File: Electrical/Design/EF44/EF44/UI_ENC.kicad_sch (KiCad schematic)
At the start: 20 parts, among them U1 74HC165, U10 74HC4051, U2 74HC165, U9 74HC4051

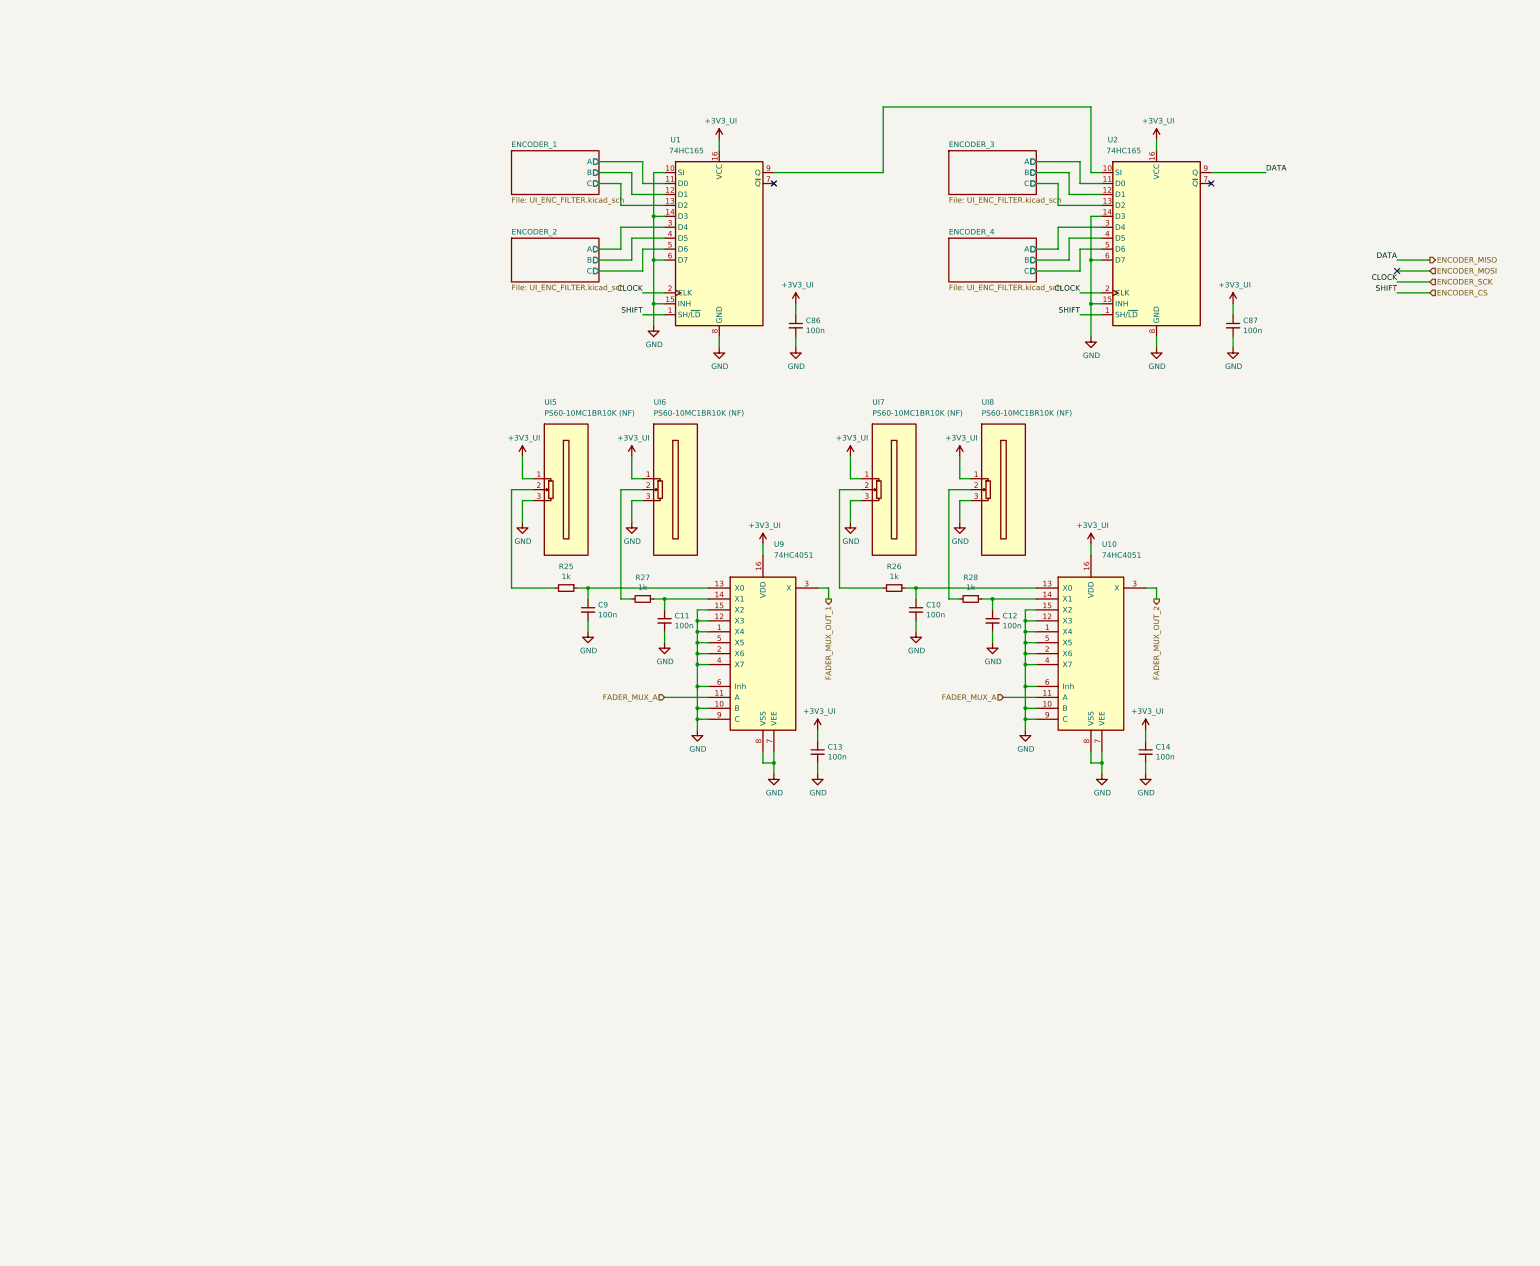
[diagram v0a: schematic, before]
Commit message: SUKU EF44 created from EN16 Base
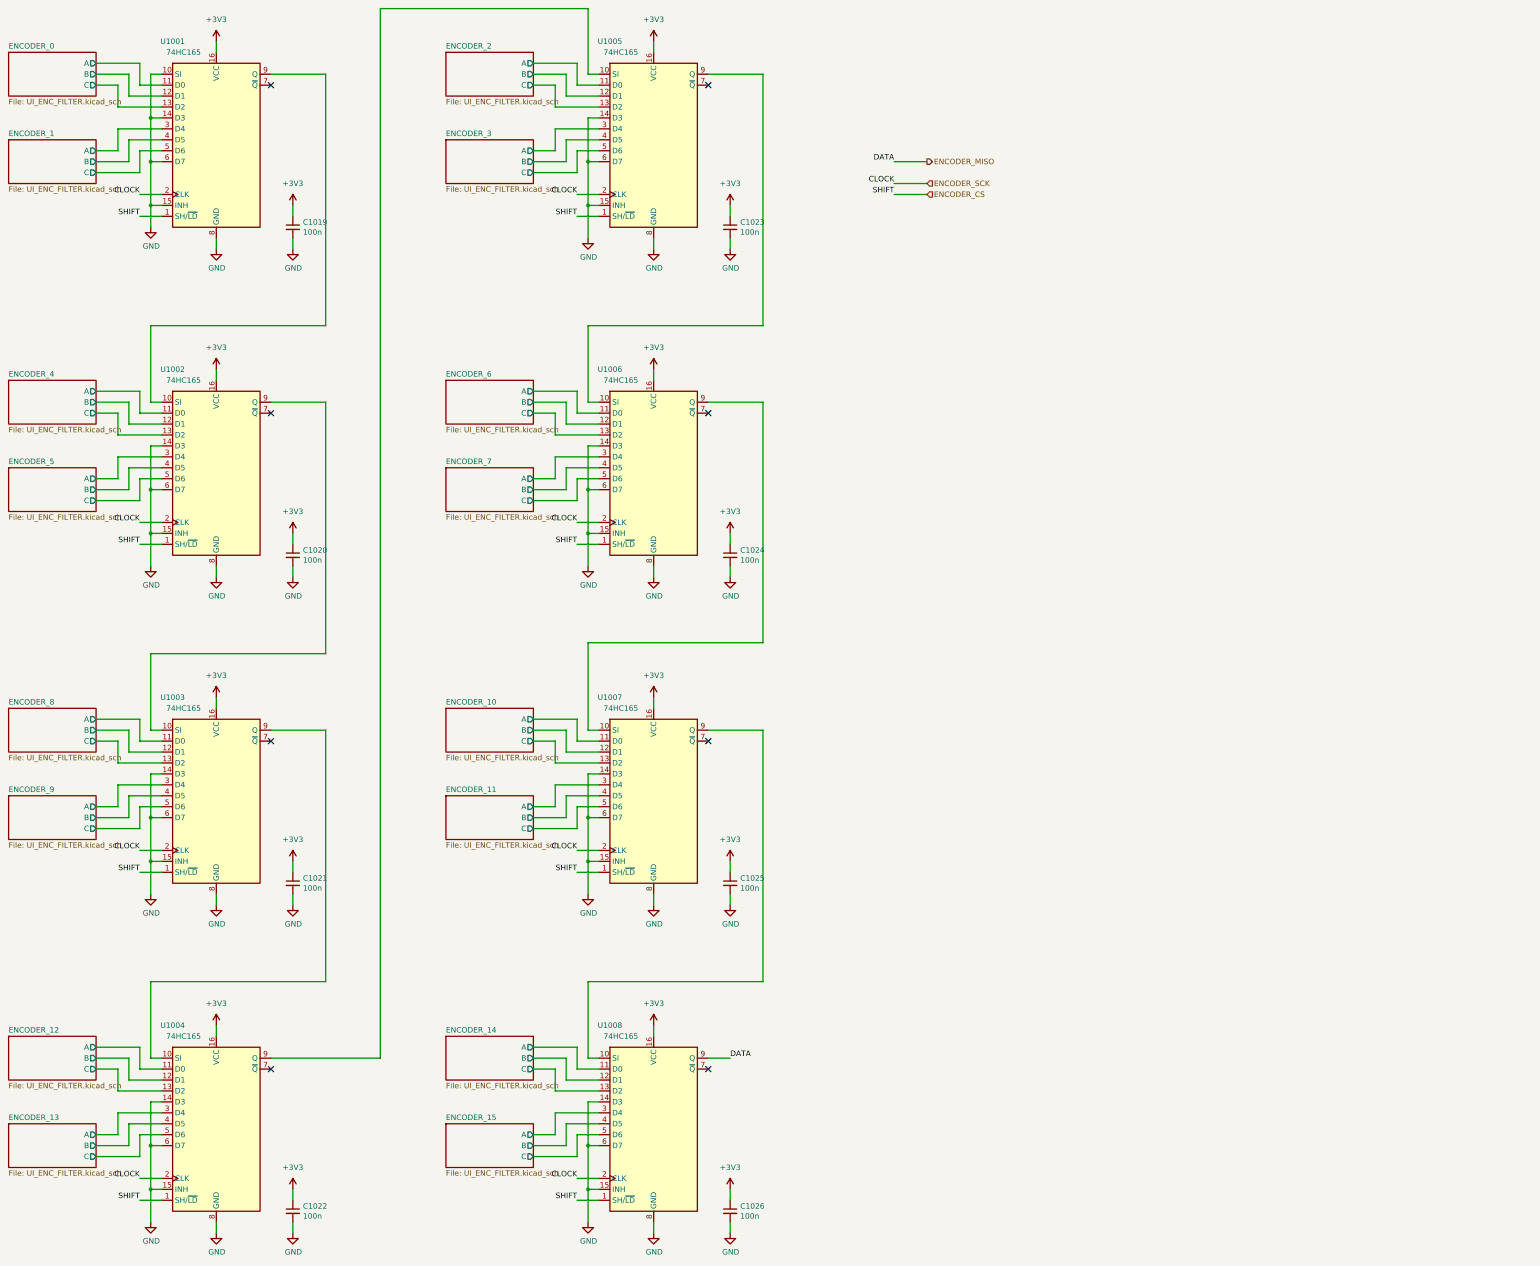
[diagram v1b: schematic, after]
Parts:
- removed C10, C11, C12, C13, C14, C9: 100n, suku_basics:CAP_0805, symbol suku_basics:CAP
- removed R25, R26, R27, R28: 1k, suku_basics:RES_0805, symbol suku_basics:RES
- removed U10, U9: 74HC4051, suku_basics:SOIC-16_74HC4051, symbol suku_basics:74HC4051
- removed UI5, UI6, UI7, UI8: PS60-10MC1BR10K (NF), suku_basics:UI_FADER_TT_long, symbol suku_basics:UI_Fader
- added C1020, C1021, C1022, C1024, C1025, C1026: 100n, suku_basics:CAP_0402, symbol suku_basics:CAP
- added U1002, U1003, U1004, U1006, U1007, U1008: 74HC165, suku_basics:SOIC-16_74HC165, symbol suku_basics:74HC165
- C1019: renamed from C86; footprint suku_basics:CAP_0805 -> suku_basics:CAP_0402
- C1023: renamed from C87; footprint suku_basics:CAP_0805 -> suku_basics:CAP_0402
- renumbered U1 to U1001, U2 to U1005
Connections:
- net ENCODER_1/A: now also U1001.3 (D4); no longer U1001.11 (D0)
- net ENCODER_1/B: now also U1001.4 (D5); no longer U1001.12 (D1)
- net ENCODER_1/C: now also U1001.5 (D6); no longer U1001.13 (D2)
- net ENCODER_2/A: now also U1005.11 (D0); no longer U1001.3 (D4)
- net ENCODER_2/B: now also U1005.12 (D1); no longer U1001.4 (D5)
- net ENCODER_2/C: now also U1005.13 (D2); no longer U1001.5 (D6)
- net ENCODER_3/A: now also U1005.3 (D4); no longer U1005.11 (D0)
- net ENCODER_3/B: now also U1005.4 (D5); no longer U1005.12 (D1)
- net ENCODER_3/C: now also U1005.5 (D6); no longer U1005.13 (D2)
- net ENCODER_4/A: now also U1002.11 (D0); no longer U1005.3 (D4)
- net ENCODER_4/B: now also U1002.12 (D1); no longer U1005.4 (D5)
- net ENCODER_4/C: now also U1002.13 (D2); no longer U1005.5 (D6)
- net ENCODER_CS: now also U1002.1 (SH/~{LD}), U1003.1 (SH/~{LD}), U1004.1 (SH/~{LD}), U1006.1 (SH/~{LD}), U1007.1 (SH/~{LD}), U1008.1 (SH/~{LD})
- net ENCODER_MISO: now also U1008.9 (Q); no longer U1005.9 (Q)
- net ENCODER_SCK: now also U1002.2 (CLK), U1003.2 (CLK), U1004.2 (CLK), U1006.2 (CLK), U1007.2 (CLK), U1008.2 (CLK)
- net GND: now also C1020.2, C1021.2, C1022.2, C1024.2, C1025.2, C1026.2, U1002.14 (D3), U1002.15 (INH), U1002.6 (D7), U1002.8 (GND), U1003.14 (D3), U1003.15 (INH), U1003.6 (D7), U1003.8 (GND), U1004.14 (D3), U1004.15 (INH), U1004.6 (D7), U1004.8 (GND), U1006.14 (D3), U1006.15 (INH), U1006.6 (D7), U1006.8 (GND), U1007.14 (D3), U1007.15 (INH), U1007.6 (D7), U1007.8 (GND), U1008.14 (D3), U1008.15 (INH), U1008.6 (D7), U1008.8 (GND)
- net at U1001.9 (Q): now also U1002.10 (SI); no longer U1005.10 (SI)
- net +3V3_UI renamed +3V3
- net +3V3: now also C1020.1, C1021.1, C1022.1, C1024.1, C1025.1, C1026.1, U1002.16 (VCC), U1003.16 (VCC), U1004.16 (VCC), U1006.16 (VCC), U1007.16 (VCC), U1008.16 (VCC)
- new net: U1002.9 (Q), U1003.10 (SI)
- new net: U1005.9 (Q), U1006.10 (SI)
- new net: U1006.9 (Q), U1007.10 (SI)
- new net: U1003.9 (Q), U1004.10 (SI)
- new net: U1007.9 (Q), U1008.10 (SI)
- new net: U1004.9 (Q), U1005.10 (SI)
- new net ENCODER_0/A: U1001.11 (D0)
- new net ENCODER_0/B: U1001.12 (D1)
- new net ENCODER_0/C: U1001.13 (D2)
- new net ENCODER_10/A: U1007.11 (D0)
- new net ENCODER_10/B: U1007.12 (D1)
- new net ENCODER_10/C: U1007.13 (D2)
- new net ENCODER_11/A: U1007.3 (D4)
- new net ENCODER_11/B: U1007.4 (D5)
- new net ENCODER_11/C: U1007.5 (D6)
- new net ENCODER_12/A: U1004.11 (D0)
- new net ENCODER_12/B: U1004.12 (D1)
- new net ENCODER_12/C: U1004.13 (D2)
- new net ENCODER_13/A: U1004.3 (D4)
- new net ENCODER_13/B: U1004.4 (D5)
- new net ENCODER_13/C: U1004.5 (D6)
- new net ENCODER_14/A: U1008.11 (D0)
- new net ENCODER_14/B: U1008.12 (D1)
- new net ENCODER_14/C: U1008.13 (D2)
- new net ENCODER_15/A: U1008.3 (D4)
- new net ENCODER_15/B: U1008.4 (D5)
- new net ENCODER_15/C: U1008.5 (D6)
- new net ENCODER_5/A: U1002.3 (D4)
- new net ENCODER_5/B: U1002.4 (D5)
- new net ENCODER_5/C: U1002.5 (D6)
- new net ENCODER_6/A: U1006.11 (D0)
- new net ENCODER_6/B: U1006.12 (D1)
- new net ENCODER_6/C: U1006.13 (D2)
- new net ENCODER_7/A: U1006.3 (D4)
- new net ENCODER_7/B: U1006.4 (D5)
- new net ENCODER_7/C: U1006.5 (D6)
- new net ENCODER_8/A: U1003.11 (D0)
- new net ENCODER_8/B: U1003.12 (D1)
- new net ENCODER_8/C: U1003.13 (D2)
- new net ENCODER_9/A: U1003.3 (D4)
- new net ENCODER_9/B: U1003.4 (D5)
- new net ENCODER_9/C: U1003.5 (D6)
- no-connect marks 3 -> 8
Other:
- added sheet ENCODER_0 (UI_ENC_FILTER.kicad_sch)
- added sheet ENCODER_10 (UI_ENC_FILTER.kicad_sch)
- added sheet ENCODER_11 (UI_ENC_FILTER.kicad_sch)
- added sheet ENCODER_12 (UI_ENC_FILTER.kicad_sch)
- added sheet ENCODER_13 (UI_ENC_FILTER.kicad_sch)
- added sheet ENCODER_14 (UI_ENC_FILTER.kicad_sch)
- added sheet ENCODER_15 (UI_ENC_FILTER.kicad_sch)
- added sheet ENCODER_5 (UI_ENC_FILTER.kicad_sch)
- added sheet ENCODER_6 (UI_ENC_FILTER.kicad_sch)
- added sheet ENCODER_7 (UI_ENC_FILTER.kicad_sch)
- added sheet ENCODER_8 (UI_ENC_FILTER.kicad_sch)
- added sheet ENCODER_9 (UI_ENC_FILTER.kicad_sch)
- moved on the sheet: C1019, C1023, U1001, U1005

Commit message: SUKU EF44 component positions done
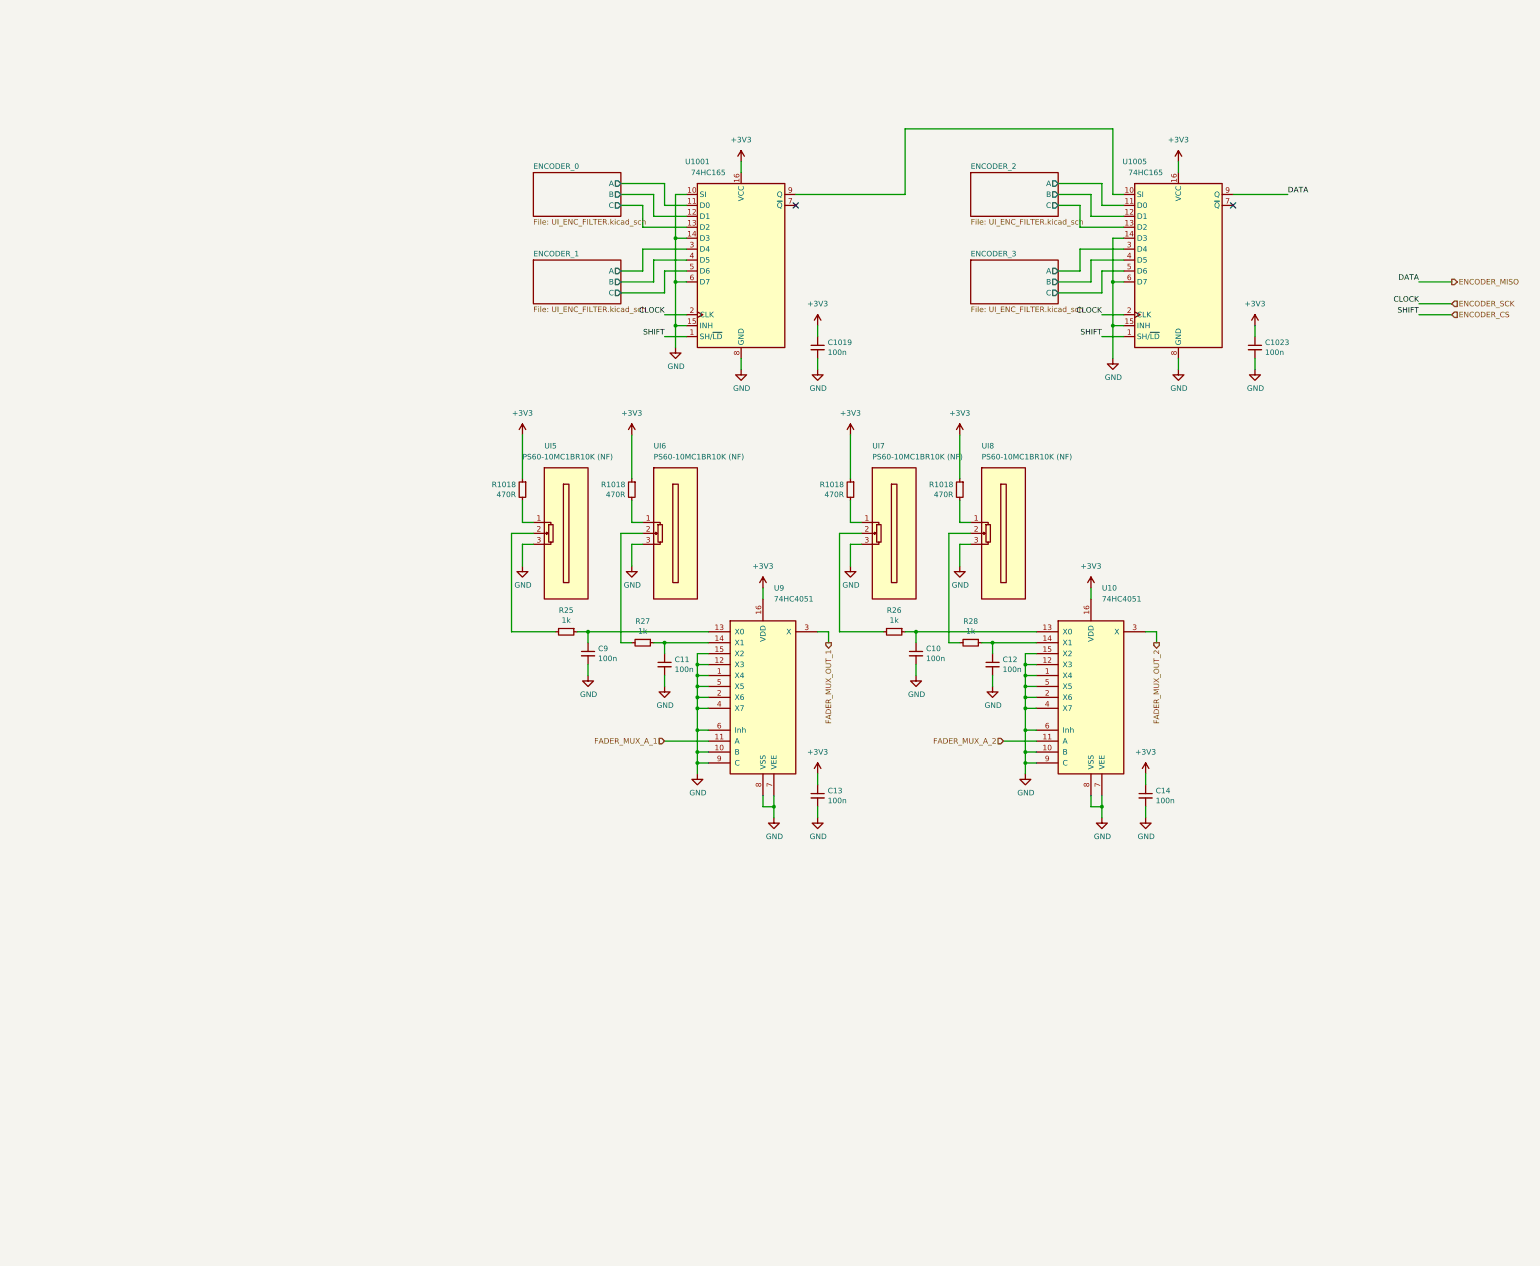
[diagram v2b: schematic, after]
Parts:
- removed C1020, C1021, C1022, C1024, C1025, C1026: 100n, suku_basics:CAP_0402, symbol suku_basics:CAP
- removed U1002, U1003, U1004, U1006, U1007, U1008: 74HC165, suku_basics:SOIC-16_74HC165, symbol suku_basics:74HC165
- added C10, C11, C12, C13, C14, C9: 100n, suku_basics:CAP_0402, symbol suku_basics:CAP
- added R1018 (x4): 470R, suku_basics:RES_0402, symbol suku_basics:RES
- added R25, R26, R27, R28: 1k, suku_basics:RES_0402, symbol suku_basics:RES
- added U10, U9: 74HC4051, suku_basics:SOIC-16_74HC4051, symbol suku_basics:74HC4051
- added UI5, UI6, UI7, UI8: PS60-10MC1BR10K (NF), suku_basics:UI_FADER_TT_long, symbol suku_basics:UI_Fader
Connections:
- net +3V3: now also C13.1, C14.1, R1018.1, R1018.1, R1018.1, R1018.1, U10.16 (VDD), U9.16 (VDD)
- net ENCODER_MISO: now also U1005.9 (Q)
- net GND: now also C10.2, C11.2, C12.2, C13.2, C14.2, C9.2, U10.1 (X4), U10.10 (B), U10.12 (X3), U10.15 (X2), U10.2 (X6), U10.4 (X7), U10.5 (X5), U10.6 (Inh), U10.7 (VEE), U10.8 (VSS), U10.9 (C), U9.1 (X4), U9.10 (B), U9.12 (X3), U9.15 (X2), U9.2 (X6), U9.4 (X7), U9.5 (X5), U9.6 (Inh), U9.7 (VEE), U9.8 (VSS), U9.9 (C), UI5.3, UI6.3, UI7.3, UI8.3
- net at U1001.9 (Q): now also U1005.10 (SI)
- new net: R1018.2, UI8.1
- new net: C9.1, R25.1, U9.13 (X0)
- new net: R25.2, UI5.2
- new net: C11.1, R27.1, U9.14 (X1)
- new net: R28.2, UI8.2
- new net: R1018.2, UI5.1
- new net: R27.2, UI6.2
- new net: C10.1, R26.1, U10.13 (X0)
- new net: R26.2, UI7.2
- new net: C12.1, R28.1, U10.14 (X1)
- new net: R1018.2, UI6.1
- new net: R1018.2, UI7.1
- new net FADER_MUX_A_1: U9.11 (A)
- new net FADER_MUX_A_2: U10.11 (A)
- new net FADER_MUX_OUT_1: U9.3 (X)
- new net FADER_MUX_OUT_2: U10.3 (X)
- no-connect marks 8 -> 2
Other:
- removed sheet ENCODER_10
- removed sheet ENCODER_11
- removed sheet ENCODER_12
- removed sheet ENCODER_13
- removed sheet ENCODER_14
- removed sheet ENCODER_15
- removed sheet ENCODER_4
- removed sheet ENCODER_5
- removed sheet ENCODER_6
- removed sheet ENCODER_7
- removed sheet ENCODER_8
- removed sheet ENCODER_9
- moved on the sheet: C1019, C1023, U1001, U1005

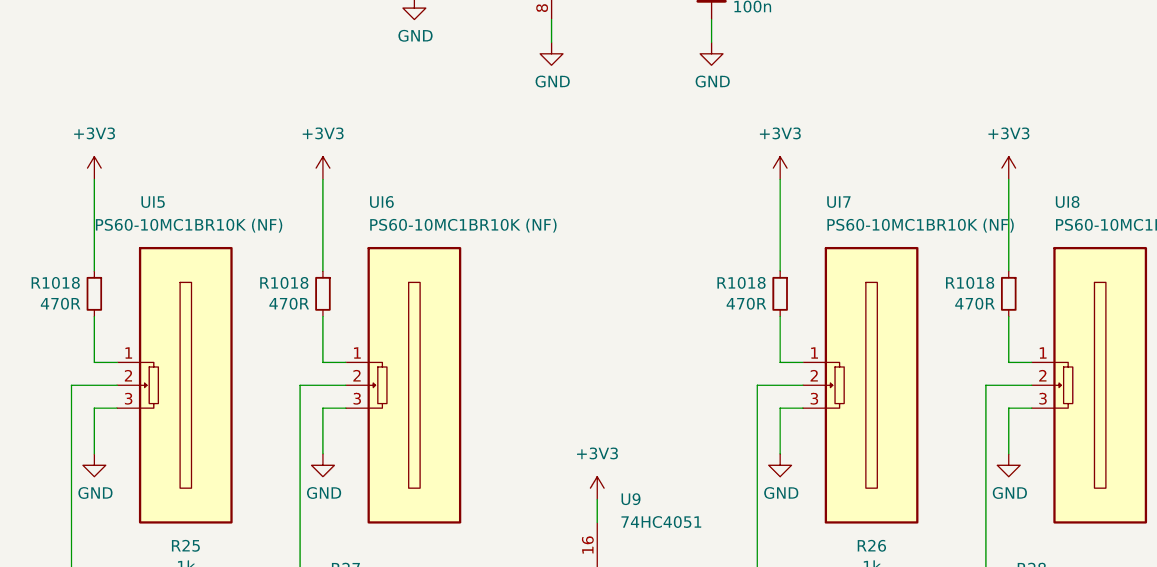
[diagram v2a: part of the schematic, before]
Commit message: SUKU EF44 routing done
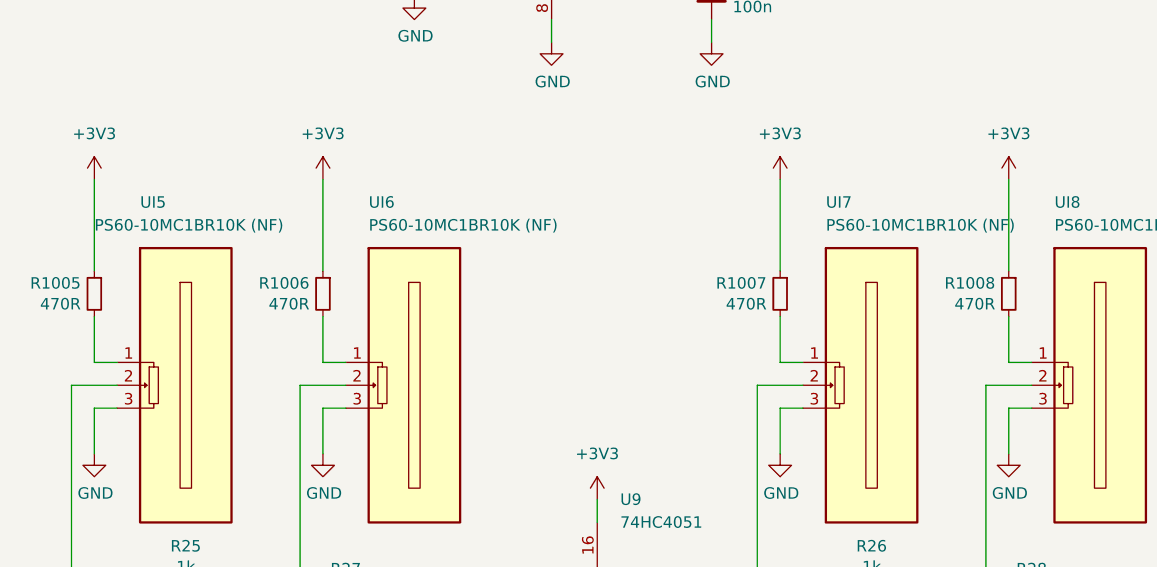
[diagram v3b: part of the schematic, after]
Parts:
- renumbered R1018 to R1005, R1018 to R1006, R1018 to R1007, R1018 to R1008
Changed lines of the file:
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@@
   (symbol (lib_id "suku_basics:RES") (at 121.92 104.14 0) (mirror y) (unit 1)
     (in_bom yes) (on_board yes) (dnp no)
-    (property "Reference" "R1018" (at 120.4214 102.9716 0)
+    (property "Reference" "R1008" (at 120.4214 102.9716 0)
       (effects (font (size 1.27 1.27)) (justify left))
     )
@@
   (symbol (lib_id "suku_basics:RES") (at 45.72 104.14 0) (mirror y) (unit 1)
     (in_bom yes) (on_board yes) (dnp no)
-    (property "Reference" "R1018" (at 44.2214 102.9716 0)
+    (property "Reference" "R1006" (at 44.2214 102.9716 0)
       (effects (font (size 1.27 1.27)) (justify left))
     )
@@
   (symbol (lib_id "suku_basics:RES") (at 20.32 104.14 0) (mirror y) (unit 1)
     (in_bom yes) (on_board yes) (dnp no)
-    (property "Reference" "R1018" (at 18.8214 102.9716 0)
+    (property "Reference" "R1005" (at 18.8214 102.9716 0)
       (effects (font (size 1.27 1.27)) (justify left))
     )
@@
   (symbol (lib_id "suku_basics:RES") (at 96.52 104.14 0) (mirror y) (unit 1)
     (in_bom yes) (on_board yes) (dnp no)
-    (property "Reference" "R1018" (at 95.0214 102.9716 0)
-      (effects (font (size 1.27 1.27)) (justify left))
-    )
+    (property "Reference" "R1007" (at 95.0214 102.9716 0)
+      (effects (font (size 1.27 1.27)) (justify left))
+    )
